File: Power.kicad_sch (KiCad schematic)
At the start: 26 parts, among them Q1 SI2301BDS, U1 BATTERY, U2 TPS63070RNMR, U3 TPRT9013-33

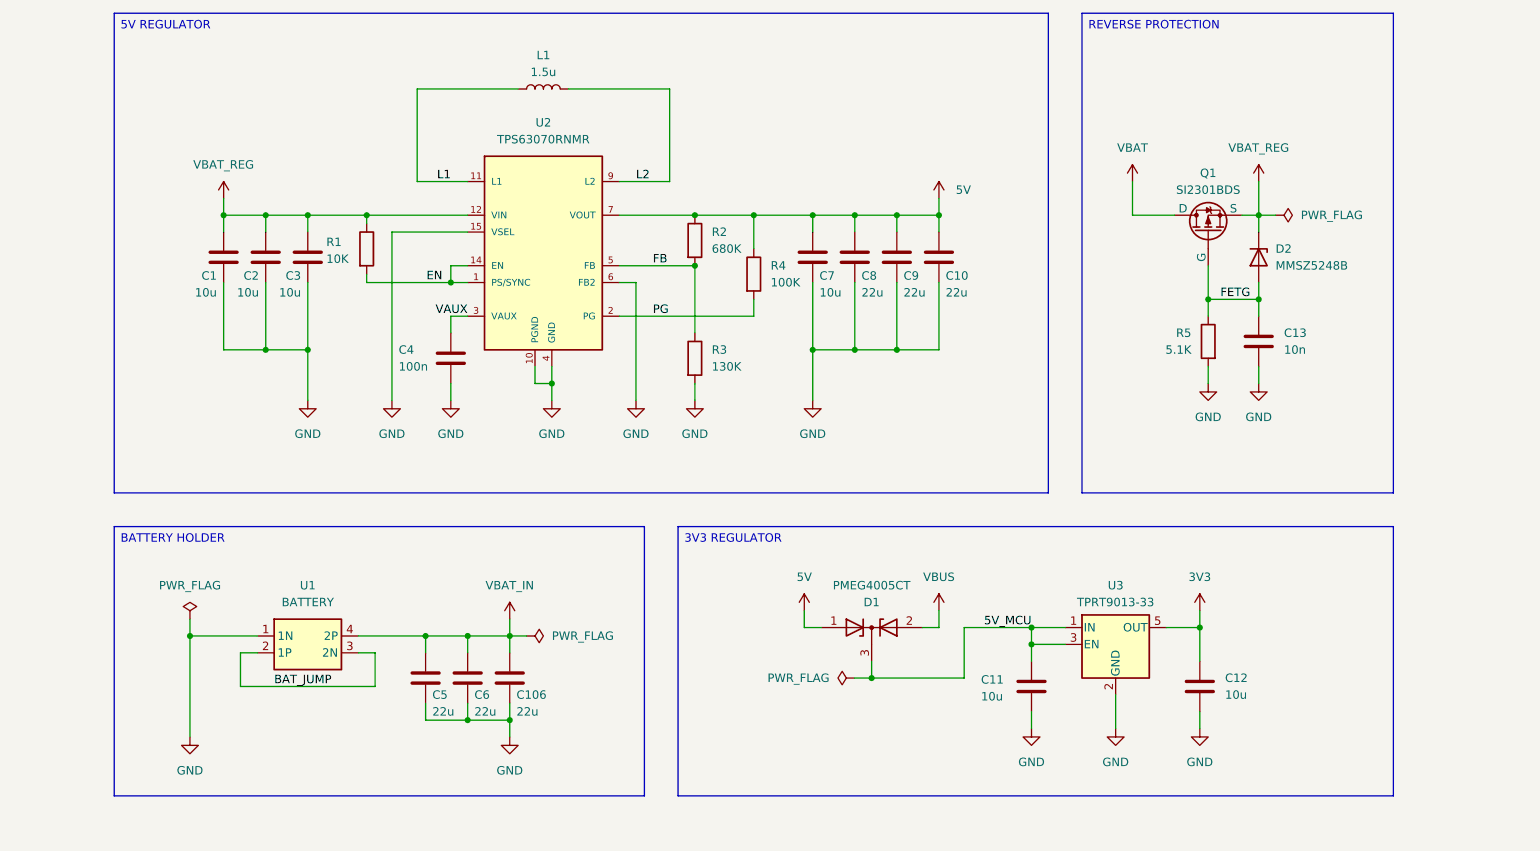
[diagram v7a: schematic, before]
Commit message: Oscillator and IMU layout
Updated the oscillator layout for the RP2350.
Updated the IMU layout for the IMU.
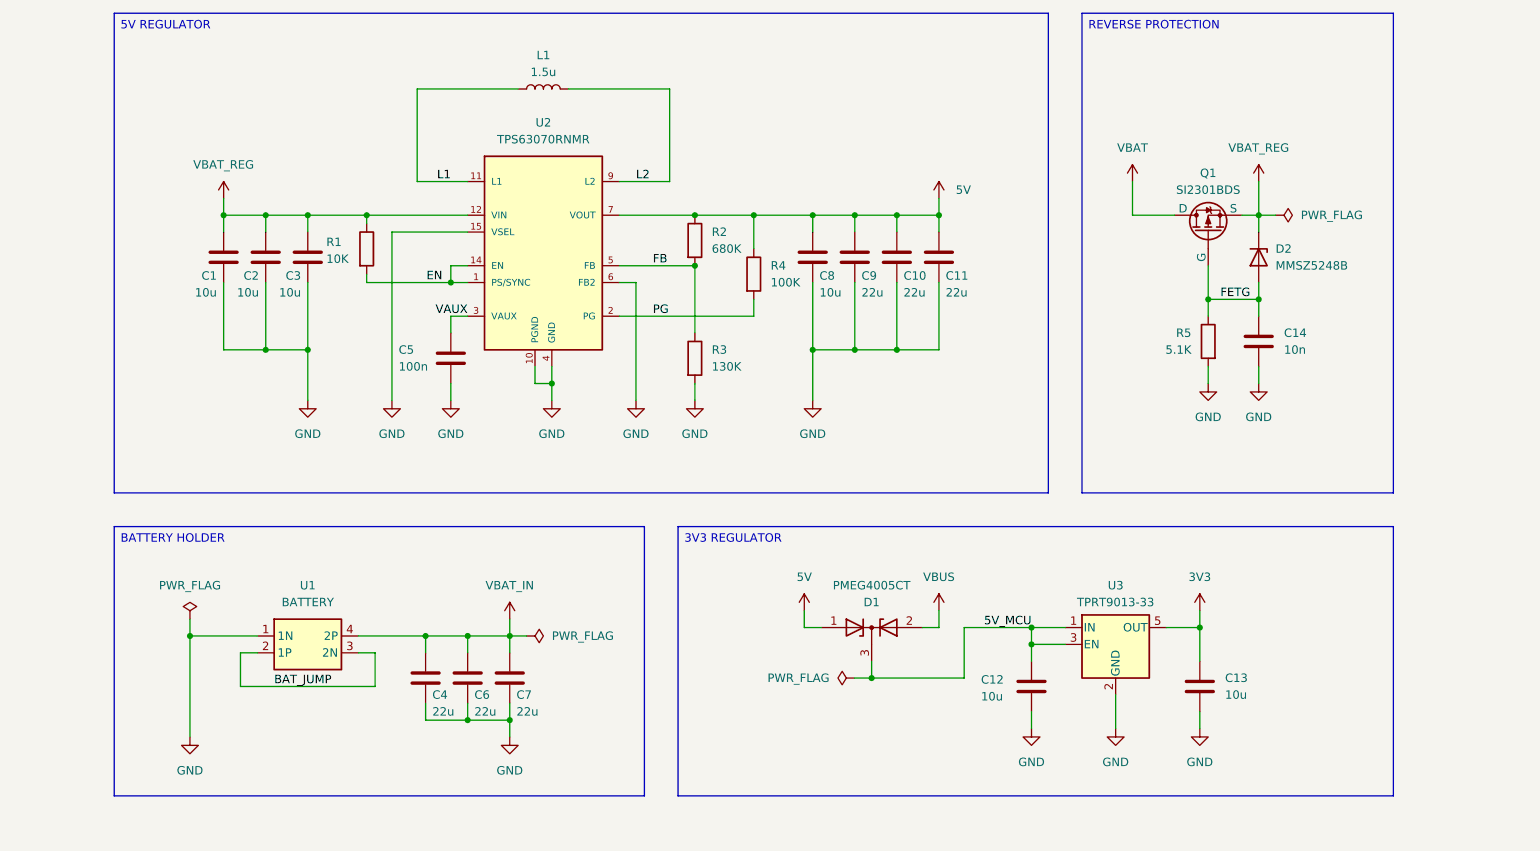
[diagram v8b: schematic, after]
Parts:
- renumbered C9 to C10, C10 to C11, C11 to C12, C12 to C13, C13 to C14, C5 to C4, C4 to C5, C106 to C7, C7 to C8, C8 to C9
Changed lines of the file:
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@@
 		(dnp no)
 		(fields_autoplaced yes)
-		(property "Reference" "C12"
+		(property "Reference" "C13"
 			(at 217.17 128.2699 0)
 			(effects
@@
 			(project "ThunderHorse"
 				(path "/ac187c6c-fa53-41cc-bce1-6f39a42a92e8/9df2a240-d97e-494f-85fd-6467f59fa68d"
-					(reference "C12")
+					(reference "C13")
 					(unit 1)
 				)
@@
 		(on_board yes)
 		(dnp no)
-		(property "Reference" "C8"
+		(property "Reference" "C9"
 			(at 162.306 67.564 0)
 			(effects
@@
 			(project "ThunderHorse"
 				(path "/ac187c6c-fa53-41cc-bce1-6f39a42a92e8/9df2a240-d97e-494f-85fd-6467f59fa68d"
-					(reference "C8")
+					(reference "C9")
 					(unit 1)
 				)
@@
 		(on_board yes)
 		(dnp no)
-		(property "Reference" "C7"
+		(property "Reference" "C8"
 			(at 155.956 67.564 0)
 			(effects
@@
 			(project "ThunderHorse"
 				(path "/ac187c6c-fa53-41cc-bce1-6f39a42a92e8/9df2a240-d97e-494f-85fd-6467f59fa68d"
-					(reference "C7")
+					(reference "C8")
 					(unit 1)
 				)
@@
 		(on_board yes)
 		(dnp no)
-		(property "Reference" "C4"
+		(property "Reference" "C5"
 			(at 92.456 78.74 0)
 			(effects
@@
 			(project ""
 				(path "/ac187c6c-fa53-41cc-bce1-6f39a42a92e8/9df2a240-d97e-494f-85fd-6467f59fa68d"
-					(reference "C4")
+					(reference "C5")
 					(unit 1)
 				)
@@
 		(on_board yes)
 		(dnp no)
-		(property "Reference" "C5"
+		(property "Reference" "C4"
 			(at 97.536 130.81 0)
 			(effects
@@
 			(project "ThunderHorse"
 				(path "/ac187c6c-fa53-41cc-bce1-6f39a42a92e8/9df2a240-d97e-494f-85fd-6467f59fa68d"
-					(reference "C5")
+					(reference "C4")
 					(unit 1)
 				)
@@
 		(on_board yes)
 		(dnp no)
-		(property "Reference" "C106"
+		(property "Reference" "C7"
 			(at 110.236 130.81 0)
 			(effects
@@
 			(project "ThunderHorse"
 				(path "/ac187c6c-fa53-41cc-bce1-6f39a42a92e8/9df2a240-d97e-494f-85fd-6467f59fa68d"
-					(reference "C106")
+					(reference "C7")
 					(unit 1)
 				)
@@
 		(on_board yes)
 		(dnp no)
-		(property "Reference" "C10"
+		(property "Reference" "C11"
 			(at 175.006 67.564 0)
 			(effects
@@
 			(project "ThunderHorse"
 				(path "/ac187c6c-fa53-41cc-bce1-6f39a42a92e8/9df2a240-d97e-494f-85fd-6467f59fa68d"
-					(reference "C10")
+					(reference "C11")
 					(unit 1)
 				)
@@
 		(dnp no)
 		(fields_autoplaced yes)
-		(property "Reference" "C13"
+		(property "Reference" "C14"
 			(at 226.06 76.1999 0)
 			(effects
@@
 			(project ""
 				(path "/ac187c6c-fa53-41cc-bce1-6f39a42a92e8/9df2a240-d97e-494f-85fd-6467f59fa68d"
-					(reference "C13")
+					(reference "C14")
 					(unit 1)
 				)
@@
 		(on_board yes)
 		(dnp no)
-		(property "Reference" "C11"
+		(property "Reference" "C12"
 			(at 180.34 128.524 0)
 			(effects
@@
 			(project "ThunderHorse"
 				(path "/ac187c6c-fa53-41cc-bce1-6f39a42a92e8/9df2a240-d97e-494f-85fd-6467f59fa68d"
-					(reference "C11")
+					(reference "C12")
 					(unit 1)
 				)
@@
 		(on_board yes)
 		(dnp no)
-		(property "Reference" "C9"
+		(property "Reference" "C10"
 			(at 168.656 67.564 0)
 			(effects
@@
 			(project "ThunderHorse"
 				(path "/ac187c6c-fa53-41cc-bce1-6f39a42a92e8/9df2a240-d97e-494f-85fd-6467f59fa68d"
-					(reference "C9")
+					(reference "C10")
 					(unit 1)
 				)
